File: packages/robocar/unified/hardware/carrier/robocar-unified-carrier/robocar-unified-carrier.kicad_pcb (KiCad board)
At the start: 2 copper layers, 166 x 102 mm, 32 parts, among them J1 IDC 2x7 head cable, J10 Piezo, J2 IDC 2x7 head cable, J3 XT30 pack in, J4 LM2596 module, J5 Motor left, J6 Motor right, J7 RCWL-1601 front, J8 RCWL-1601 rear, J9 SSD1306 0.91in, U1 XIAO ESP32-S3 Sense, U2 AMS1117-3.3

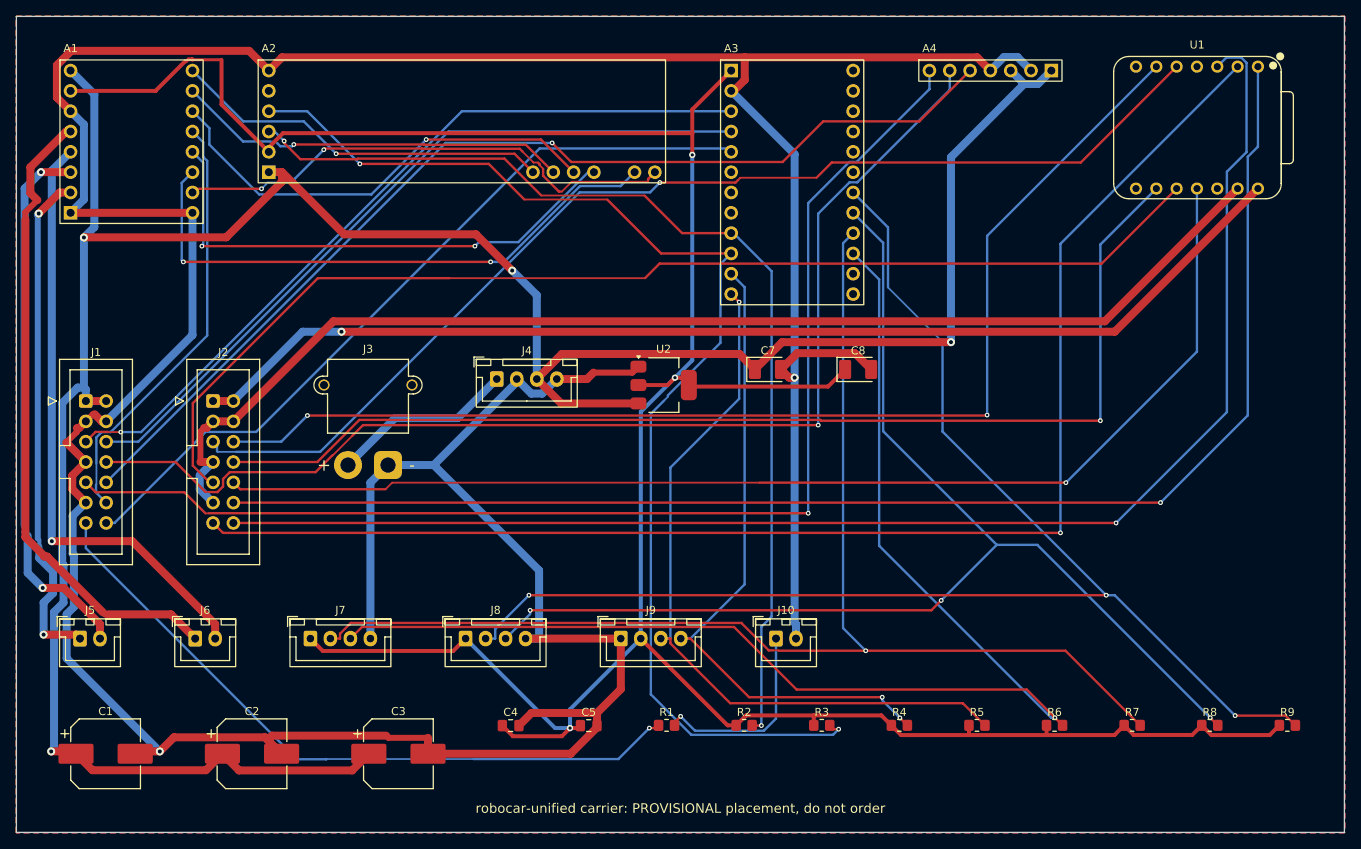
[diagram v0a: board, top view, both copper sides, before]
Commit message: feat(robocar-unified): combined head and main outline and placement
Replaces #793's row-packed stand-in with a layout: one 100 x 100 mm
rectangle holding the main board and, in the top-right corner, the head
board for the pan-tilt cradle. A 3 mm keepout band under a silkscreen saw
line separates them, so JLCPCB sees a single design and Lauri saws the
head off after delivery.

- Head (30 x 34 mm): the XIAO socket with USB-C at the outer edge, J2
  lying along the bottom edge so the ribbon folds toward the pan axis, and
  two M2 holes for the cradle. It is wider than the planned 24 mm because
  the shrouded 2x7 header is 26.4 mm long.
- Main: M3 holes at its four corners. The TB6612 sits at the left edge,
  with the left motor lead below it and the right motor lead on the right
  edge. J1 is beside the band at the pan-tilt end. Power in, the buck lead,
  the rear rangefinder and the piezo are on the rear edge, and the front
  rangefinder and the OLED lead on the front edge. Each decoupling or bulk
  capacitor is beside the part it serves.
- HEAD_GND gets its own pour region on the head; GND pours the main board.
  The .kicad_dru single-spoke rule now covers both nets.
- Mounting holes are carrier parts, as on balancebot: H1-H4 M3, and H5-H6
  M2 from a new m2-mounting-hole registry entry with its vendored footprint.
- [project] paper is A2, the sheet the schematic writer grows to.

Every dimension is provisional and its board.toml comment says what to
measure. The cradle plate, the chassis plate and the ribbon length are
still unmeasured. The board is routed by Freerouting only so the carrier
gates have a routed board to check; the header still says not to order
it.

Part of #750.

Co-Authored-By: Claude Opus 5.5 <noreply@anthropic.com>
Claude-Session: https://claude.ai/code/session_01LmLtwHDbHDLXFMLxCn3smf
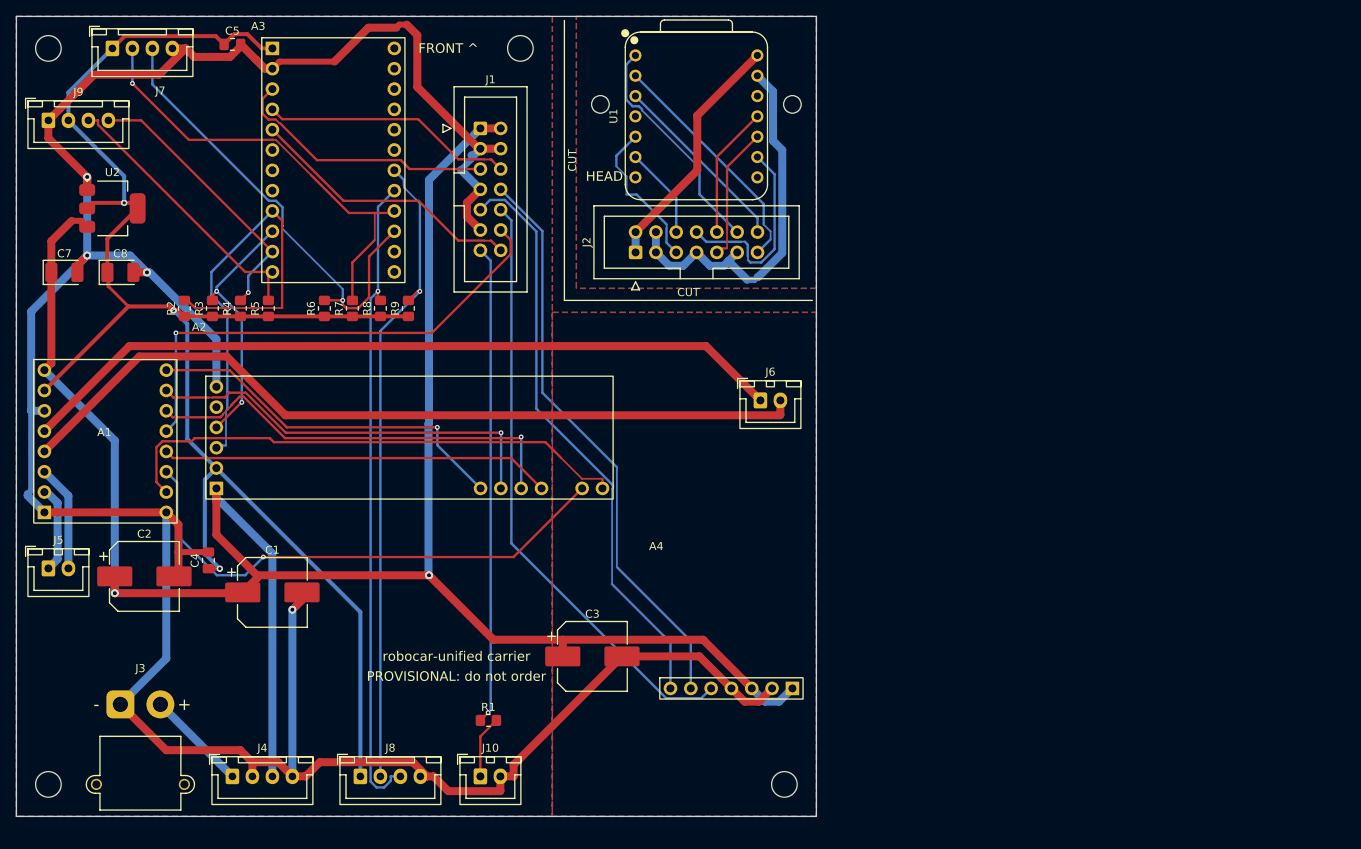
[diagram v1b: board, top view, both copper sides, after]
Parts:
- added H1: M3, MountingHole:MountingHole_3.2mm_M3, F.Cu at (104.0, 104.0)
- added H2: M3, MountingHole:MountingHole_3.2mm_M3, F.Cu at (163.0, 104.0)
- added H3: M3, MountingHole:MountingHole_3.2mm_M3, F.Cu at (104.0, 196.0)
- added H4: M3, MountingHole:MountingHole_3.2mm_M3, F.Cu at (196.0, 196.0)
- added H5: M2, MountingHole:MountingHole_2.2mm_M2, F.Cu at (173.0, 111.0)
- added H6: M2, MountingHole:MountingHole_2.2mm_M2, F.Cu at (197.0, 111.0)
- moved R9 121.6 mm to (149.0, 136.5), turned to 90 degrees
- moved R8 116.0 mm to (145.5, 136.5), turned to 90 degrees
- moved R7 110.5 mm to (142.0, 136.5), turned to 90 degrees
- moved R6 105.1 mm to (138.5, 136.5), turned to 90 degrees
- moved R5 102.8 mm to (131.5, 136.5), turned to 90 degrees
- moved R4 97.5 mm to (128.0, 136.5), turned to 90 degrees
- moved J9 96.5 mm to (104.0, 113.0)
- moved C5 96.1 mm to (127.0, 103.5)
- moved C8 93.0 mm to (113.0, 132.0)
- moved R3 92.3 mm to (124.5, 136.5), turned to 90 degrees
- moved C7 88.8 mm to (106.0, 132.0)
- moved R2 87.2 mm to (121.0, 136.5), turned to 90 degrees
- moved A4 83.7 mm to (197.0, 184.0)
- moved J7 77.8 mm to (112.0, 104.0)
- moved J6 76.7 mm to (193.0, 148.0)
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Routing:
- net GND: track 527.6 -> 359.2 mm, vias 2 -> 4
- net HEAD_MUX_RST: track 179.0 -> 23.3 mm, vias 1 -> 0
- net HEAD_MOTOR_STBY: track 175.4 -> 28.8 mm, vias 1 -> 0
- net +3V3: track 348.1 -> 202.3 mm
- net HEAD_PIEZO: track 173.9 -> 29.8 mm, vias 1 -> 0
- net HEAD_I2C_SCL: track 147.9 -> 11.5 mm, vias 2 -> 0
- net HEAD_I2S_DIN: track 148.3 -> 16.6 mm, vias 1 -> 0
- net HEAD_I2S_LRCLK: track 145.3 -> 17.0 mm
- net HEAD_I2C_SDA: track 141.3 -> 19.3 mm, vias 1 -> 0
- net CH0_SCL: track 151.6 -> 31.4 mm
- net HEAD_I2S_BCLK: track 142.5 -> 25.6 mm, vias 1 -> 0
- net HEAD_+5V: track 141.6 -> 30.9 mm, vias 1 -> 0
- net HEAD_GND: track 154.1 -> 48.0 mm
- net CH3_SCL: track 161.6 -> 56.0 mm
- net CH3_SDA: track 163.5 -> 58.3 mm
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- added copper zone on B.Cu, net HEAD_GND
- added copper zone on F.Cu, net HEAD_GND
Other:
- board size 166 x 102 mm -> 100 x 100 mm
- board text added: "CUT"
- board text added: "FRONT ^"
- board text added: "HEAD"
- board text added: "PROVISIONAL: do not order"
- board text added: "robocar-unified carrier"
- board text removed: "robocar-unified carrier: PROVISIONAL placement, do not order"

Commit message: fix(robocar-unified): fit the head board to the 30 mm pan-tilt cradle (#795)
* feat(kicad): place a carrier footprint on the back face

robocar-unified's head board carries its IDC ribbon header on the back,
and board.toml had no way to say so. A [placement] entry may now end in
"back": build_board.py flips the footprint about its anchor after adding
it to the board (Flip() before Add() segfaults) and then sets the
rotation as seen from the top. boardcheck accepts only "back" as the
fourth element.

Co-Authored-By: Claude Opus 5.5 <noreply@anthropic.com>
Claude-Session: https://claude.ai/code/session_01LmLtwHDbHDLXFMLxCn3smf

* fix(robocar-unified): fit the head board to the 30 mm pan-tilt cradle

Lauri measured the cradle's inner width at 30.0 mm. The head was 30 mm of
copper with the saw line 1.5 mm outside it, so it would have come out
about 31 mm wide. The saw line now sits at x 70.5, making the head 29.5 mm
wide (0.25 mm per side), with the 3 mm band at x 69-72.

At 28 mm of copper the two M2 holes no longer fit beside the XIAO. Per
Lauri, they move above it, either side of the USB-C, and the IDC header
J2 goes on the back face under the XIAO's lower end. The head grows from
34 to about 38.5 mm (provisional until the cradle's inner height and screw
positions are measured). A2 and C4 move down 1 mm to clear the lowered band.

Board re-placed and re-routed with carrier-board; carrier-check passes
and wrote the stamp. Still provisional: do not order.

Co-Authored-By: Claude Opus 5.5 <noreply@anthropic.com>
Claude-Session: https://claude.ai/code/session_01LmLtwHDbHDLXFMLxCn3smf

---------

Co-authored-by: Claude Opus 5.5 <noreply@anthropic.com>
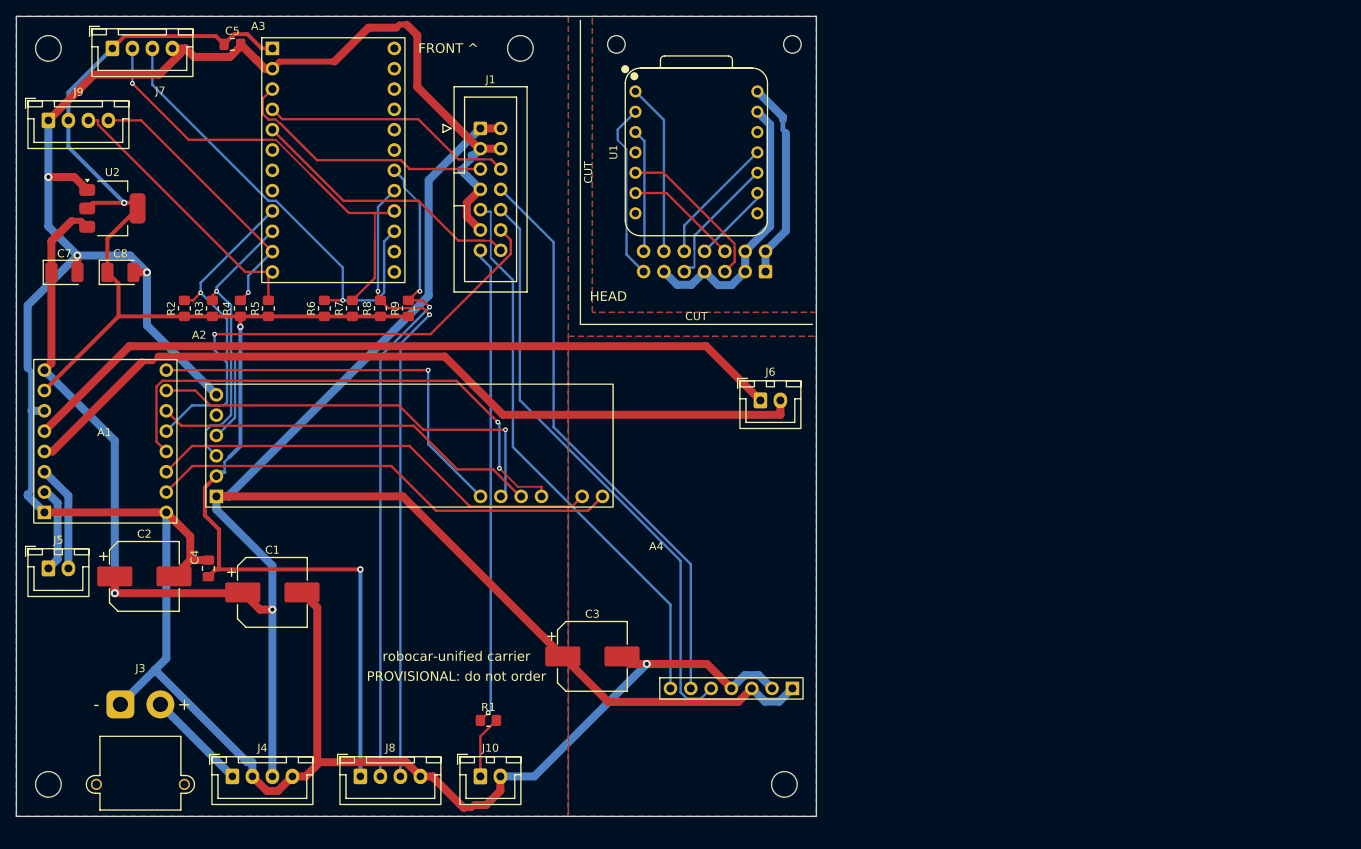
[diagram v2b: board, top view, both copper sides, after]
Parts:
- J2: moved to B.Cu
- moved J2 16.4 mm to (193.6, 131.9)
- moved H5 7.76 mm to (175.0, 103.5)
- moved H6 7.50 mm to (197.0, 103.5)
- moved U1 4.50 mm to (185.0, 117.0)
- moved A2 1.00 mm to (125.0, 160.0)
- moved C4 1.00 mm to (124.0, 169.0)
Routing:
- net CH0_SDA: track 60.0 -> 40.9 mm, vias 0 -> 1
- net BIN1: track 48.8 -> 67.0 mm, vias 0 -> 2
- net HEAD_I2S_BCLK: track 25.6 -> 10.0 mm
- net HEAD_GND: track 48.0 -> 34.9 mm
- net BIN2: track 65.7 -> 57.0 mm, vias 1 -> 0
- net HEAD_MUX_RST: track 23.3 -> 15.4 mm
- net HEAD_PIEZO: track 29.8 -> 22.2 mm
- net HEAD_MOTOR_STBY: track 28.8 -> 21.5 mm
- net PWMB: track 65.6 -> 58.9 mm
- net HEAD_+5V: track 30.9 -> 25.1 mm
- net AIN1: track 54.5 -> 48.8 mm, vias 1 -> 0
- net PWMA: track 46.7 -> 51.2 mm
- net GND: track 359.2 -> 363.6 mm
- net +3V3: track 202.3 -> 198.4 mm
- net I2S_LRCLK: track 73.3 -> 70.3 mm
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
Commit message: fix(robocar-unified): fit the head board to the 30 x 30 mm cradle (#797)
* fix(kicad): set a back-side part's silk after flipping it

build_board.py applied [silk] ref_positions before the flip, so the flip
mirrored the label with the footprint: J2's reference landed at y 15.04
instead of the 21.0 board.toml asked for. The flip now comes straight
after Add(), before any silk. A test pins the stored reference offset,
and fails with the old order.

Co-Authored-By: Claude Opus 5.5 <noreply@anthropic.com>
Claude-Session: https://claude.ai/code/session_01LmLtwHDbHDLXFMLxCn3smf

* fix(robocar-unified): fit the head board to the 30 x 30 mm cradle

Lauri measured the cradle's inner height at 30.0 mm as well as its width,
so the head is sawn to 29.5 x 29.5 mm: copper x 72-100, y 0-28, with the
3 mm band and saw lines at x 70.5 and y 29.5.

The XIAO socket and the shrouded IDC header (26.5 mm long) no longer fit
together in 28 mm, with or without the M2 holes. Lauri's choice: J2 and J1
become unshrouded 2x7 pin headers (one registry entry serves both ends),
J2 on the back face beside the XIAO, and the M2 holes go in the two bottom
corners. The ribbon plug is unkeyed on a pin header; the footprint's pin-1
mark carries the orientation on both faces.

HEAD_+5V and HEAD_GND move to the 0.5 mm logic_power class: 1 mm tracks
do not route between the head's pads, and the XIAO and camera draw well
under 1 A. Freerouting also routed head tracks onto the edge, inside
KiCad's 0.5 mm copper-to-edge rule, so 0.5 mm keepouts now line the top,
left and right edges (not the bottom, where J3's courtyard meets it).
The band's move frees the main board's corner, so A2 and C4 return to
their #794 positions.

Board re-placed and re-routed with carrier-board; carrier-check passes
and wrote the stamp. Still provisional: do not order.

Co-Authored-By: Claude Opus 5.5 <noreply@anthropic.com>
Claude-Session: https://claude.ai/code/session_01LmLtwHDbHDLXFMLxCn3smf

* fix(robocar-unified): put the head'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
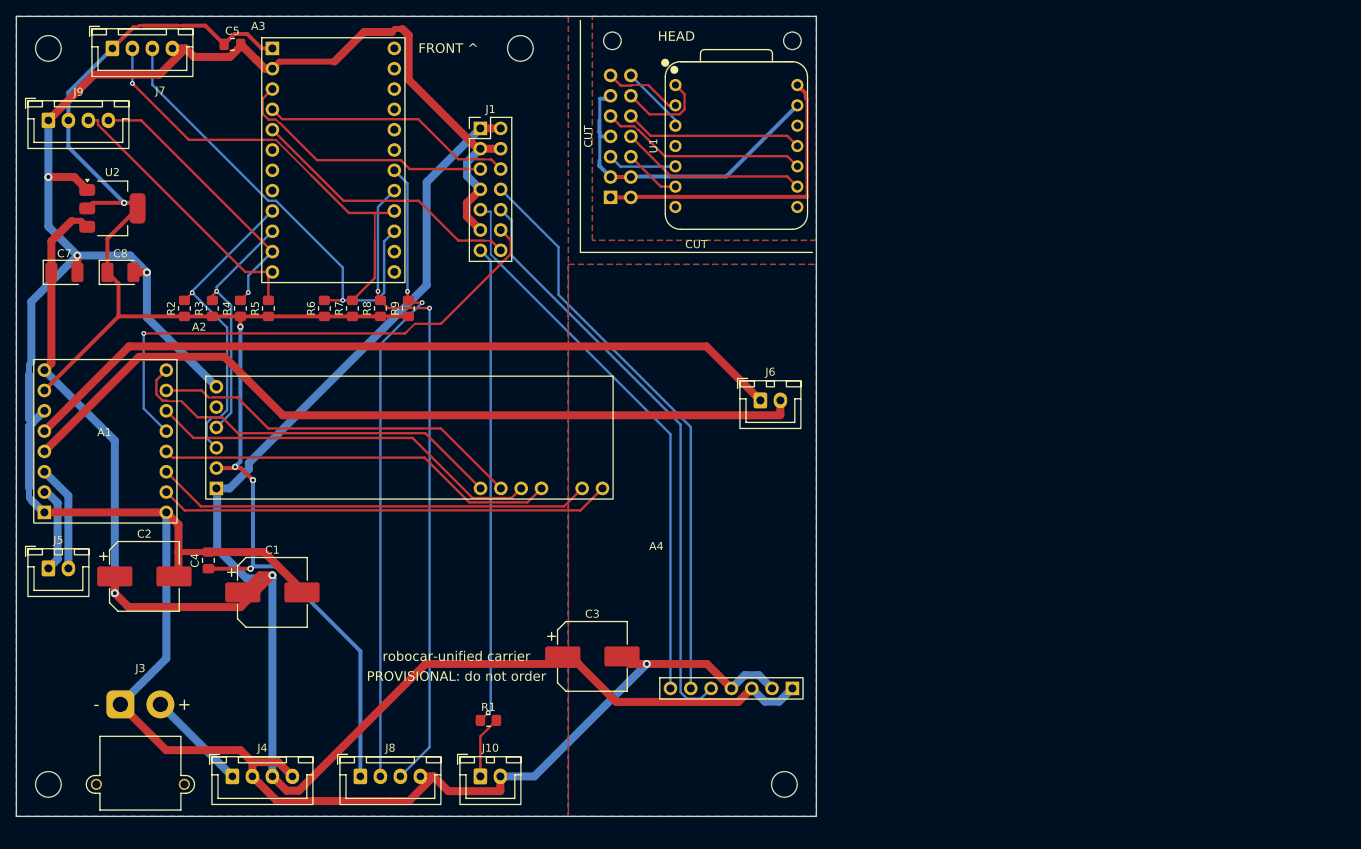
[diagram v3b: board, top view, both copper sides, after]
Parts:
- J1, J2: footprint Connector_IDC:IDC-Header_2x07_P2.54mm_Vertical -> Connector_PinHeader_2.54mm:PinHeader_2x07_P2.54mm_Vertical
- moved J2 21.5 mm to (174.3, 122.6), turned to 0 degrees
- moved U1 5.06 mm to (190.0, 116.2)
- moved A2 1.00 mm to (125.0, 159.0)
- moved C4 1.00 mm to (124.0, 168.0)
- moved H5 0.67 mm to (174.5, 103.0)
- moved H6 0.45 mm to (197.0, 103.0)
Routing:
- net BIN1: track 67.0 -> 50.3 mm, vias 2 -> 0
- net HEAD_+5V: track 25.1 -> 39.1 mm
- net HEAD_I2S_BCLK: track 10.0 -> 23.4 mm
- net HEAD_PIEZO: track 22.2 -> 9.72 mm
- net HEAD_I2C_SDA: track 20.1 -> 8.64 mm
- net HEAD_MOTOR_STBY: track 21.5 -> 11.4 mm
- net HEAD_I2S_LRCLK: track 16.6 -> 26.0 mm
- net HEAD_I2C_SCL: track 14.2 -> 7.12 mm
- net HEAD_MUX_RST: track 15.4 -> 8.59 mm
- net HEAD_I2S_DIN: track 16.1 -> 22.4 mm
- net AIN2: track 53.0 -> 46.9 mm, vias 1 -> 0
- net HEAD_GND: track 34.9 -> 40.3 mm
- net +3V3: track 198.4 -> 194.1 mm, vias 3 -> 5
- net MOTOR_STBY: track 62.9 -> 66.9 mm
- net GND: track 363.6 -> 360.8 mm
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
